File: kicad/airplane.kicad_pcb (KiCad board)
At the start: 2 copper layers, 23 parts, among them M1 Ailerons, M2 Elevator, M3 Rudder, M4 Wheel, U1 ESP32_DevKit, U10 L7805, U11 BMP280, U12 NEO-6M_GPS, U13 SD_Module, U2 nRF24L01+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

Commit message: airplane full pcb done
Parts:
- removed C5, C6: 10uF, Capacitor_THT:CP_Radial_D4.0mm_P1.50mm
- added G***: LOGO, airplane_foots:F18, F.Cu at (109.5, 84.2)
- added R1: 330, Resistor_THT:R_Axial_DIN0204_L3.6mm_D1.6mm_P5.08mm_Horizontal, F.Cu at (142.2, 116.5)
- added R2: 330, Resistor_THT:R_Axial_DIN0204_L3.6mm_D1.6mm_P5.08mm_Horizontal, F.Cu at (145.3, 116.5)
- added R3: 330, Resistor_THT:R_Axial_DIN0204_L3.6mm_D1.6mm_P5.08mm_Horizontal, F.Cu at (148.5, 116.5)
- added R4: 330, Resistor_THT:R_Axial_DIN0204_L3.6mm_D1.6mm_P5.08mm_Horizontal, F.Cu at (151.7, 116.5)
- U10: value L7805 -> AMS1117-3.3; footprint Package_TO_SOT_THT:TO-220-3_Vertical -> Connector_PinHeader_2.54mm:PinHeader_1x03_P2.54mm_Vertical
- moved U1 169.4 mm to (192.1, 111.8), turned to 90 degrees
- moved U3 158.2 mm to (200.7, 84.7)
- moved M1 155.1 mm to (178.7, 89.8), turned to 180 degrees
- moved U2 146.8 mm to (218.7, 87.8)
- moved M2 146.0 mm to (174.1, 89.8), turned to 180 degrees
- moved U4 142.6 mm to (189.7, 84.7)
- moved M3 136.9 mm to (169.5, 89.8), turned to 180 degrees
- moved M4 127.8 mm to (164.9, 89.8), turned to 180 degrees
- moved C1 106.6 mm to (154.0, 98.8)
- moved C2 101.2 mm to (154.2, 82.8)
- moved U8 99.0 mm to (126.7, 122.2)
- moved C3 94.2 mm to (144.7, 98.8)
- moved C4 90.5 mm to (144.7, 82.8)
- moved U13 70.6 mm to (113.2, 94.2), turned to 180 degrees
- moved U10 66.6 mm to (156.2, 108.8), turned to 180 degrees
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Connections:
- C1 pad 1: Net-(U10-IN) -> Net-(U10-VI)
- C3 pad 1: Net-(U10-IN) -> Net-(U10-VI)
- U10 pad 1: Net-(U10-IN) -> GND
- U10 pad 2: GND -> Net-(U10-VO)
- U10 pad 3: Net-(U10-OUT) -> Net-(U10-VI)
- U11 pad 1: Net-(U10-OUT) -> Net-(U10-VO)
- U11 pad 5: Net-(U10-OUT) -> Net-(U10-VO)
- U12 pad 1: Net-(U10-OUT) -> Net-(U10-VO)
- U13 pad 2: unconnected-(U13-3V3-Pad2) -> Net-(U10-VO)
- U13 pad 3: Net-(U10-OUT) -> unconnected-(U13-5V-Pad3)_1
- U5 pad 2: Net-(U10-IN) -> Net-(U10-VI)
- U6 pad 1: Net-(U10-IN) -> Net-(U10-VI)
- U6 pad 2: GND -> Net-(M1-+)
- U6 pad 3: Net-(M1-+) -> GND
- U7 pad 1: Net-(U10-IN) -> Net-(U10-VI)
- U7 pad 2: GND -> Net-(M3-+)
- U7 pad 3: Net-(M3-+) -> GND
- U8 pad 2: GND -> Net-(U8-GNDR)
- U8 pad 4: GND -> Net-(U8-GNDG)
- U8 pad 6: GND -> Net-(U8-GND1)
- U8 pad 8: GND -> Net-(U8-GND2)
- U9 pad 1: Net-(U10-OUT) -> Net-(U10-VO)
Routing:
- net Net-(U1-GPIO16): track 0.00 -> 137.5 mm
- net Net-(U1-GPIO17): track 0.00 -> 136.3 mm
- net Net-(U10-VO): track 0.00 -> 132.6 mm
- net Net-(U1-GPIO19): track 0.00 -> 103.2 mm, vias 0 -> 2
- net Net-(U1-GPIO18): track 0.00 -> 102.8 mm, vias 0 -> 1
- net Net-(U1-GPIO21): track 0.00 -> 95.5 mm
- net Net-(U1-GPIO22): track 0.00 -> 87.7 mm
- net Net-(U1-GPIO23): track 0.00 -> 83.7 mm, vias 0 -> 1
- net Net-(U1-GPIO5): track 0.00 -> 78.9 mm, vias 0 -> 1
- net Net-(U1-VIN): track 0.00 -> 73.4 mm
- net Net-(U10-VI): track 0.00 -> 73.2 mm
- net Net-(M1-PWM): track 0.00 -> 70.0 mm
- net Net-(U1-GPIO26): track 0.00 -> 70.0 mm, vias 0 -> 1
- net Net-(M2-PWM): track 0.00 -> 64.3 mm
- net Net-(M3-PWM): track 0.00 -> 63.7 mm
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- added copper zone on B.Cu, net GND
- added copper zone on F.Cu, net GND
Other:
- board outline added: 120 x 50 mm
- board text added: "Final Project - Airplane Breno Soares Alves"
- board text added: "M1: Ailerons - GPIO13 M2: Elevator - GPIO12 M3, M4: R&W - GPIO14 U4: PWM - GPIO15 U8: Nav - GPIO26 U8: Strobe - GPIO27 U13: CS - GPIO5 U2: CE - GPIO4 U2: CSN - GPIO15"

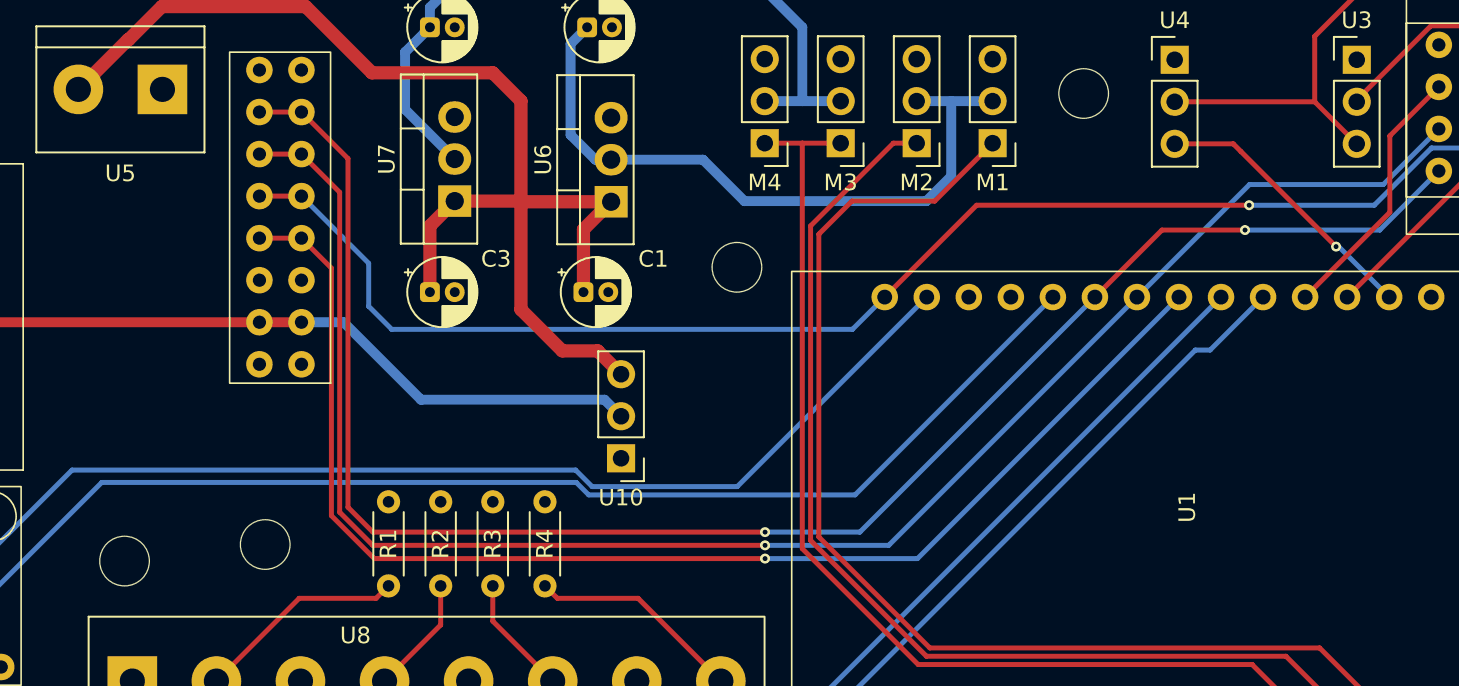
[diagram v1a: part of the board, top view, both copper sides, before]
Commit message: remote control schematic done, waiting revision
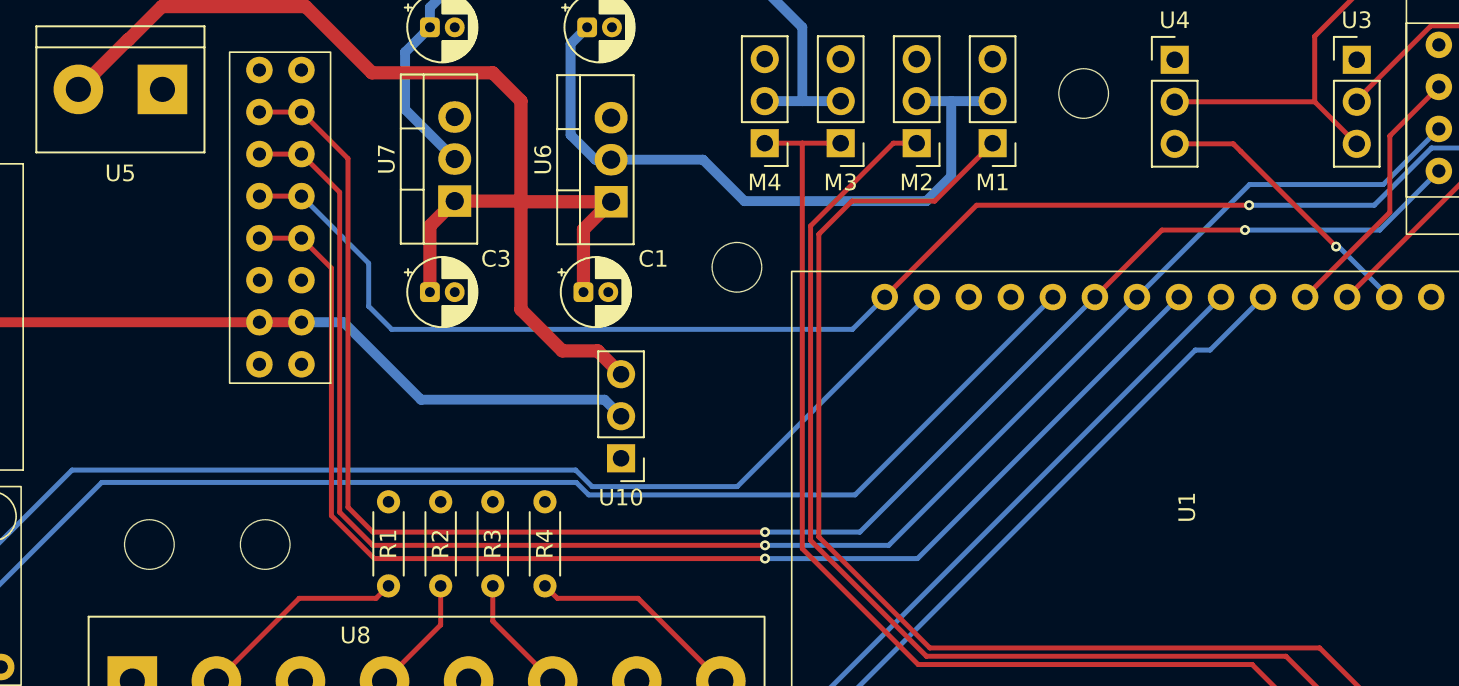
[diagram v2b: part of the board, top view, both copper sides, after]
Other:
- outline, holes or cut-outs redrawn
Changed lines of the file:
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@@
 		)
 		(embedded_fonts no)
+		(model "${KIPRJMOD}/3d/bmp280_module.stp"
+			(offset
+				(xyz 3.5 -4.75 27.5)
+			)
+			(scale
+				(xyz 1 1 1)
+			)
+			(rotate
+				(xyz -90 -0 90)
+			)
+		)
 	)
 	(footprint "Connector_PinHeader_2.54mm:PinHeader_1x03_P2.54mm_Vertical"
@@
 	)
 	(gr_circle
-		(center 126.25 115)
-		(end 127.75 115)
+		(center 127.75 114)
+		(end 129.25 114)
 		(stroke
 			(width 0.05)
@@
 	)
 	(segment
-		(start 198.16 87.25)
-		(end 189.7 87.25)
+		(start 210.2 121.99)
+		(end 210.2 82.25)
 		(width 0.3)
 		(layer "F.Cu")
@@
 	)
 	(segment
-		(start 210.2 121.99)
-		(end 210.2 82.25)
+		(start 189.7 87.25)
+		(end 198.16 87.25)
 		(width 0.3)
 		(layer "F.Cu")
@@
 	)
 	(segment
-		(start 200.7 89.79)
-		(end 198.16 87.25)
+		(start 207.74 124.45)
+		(end 210.2 121.99)
 		(width 0.3)
 		(layer "F.Cu")
@@
 	)
 	(segment
-		(start 207.74 124.45)
-		(end 210.2 121.99)
+		(start 198.16 87.25)
+		(end 200.7 89.79)
 		(width 0.3)
 		(layer "F.Cu")
@@
 	)
 	(segment
-		(start 207.049 82.659)
-		(end 208.2 83.81)
+		(start 200.7 87.25)
+		(end 200.7 87.14224)
 		(width 0.3)
 		(layer "F.Cu")
@@
 	)
 	(segment
-		(start 205.18324 82.659)
-		(end 207.049 82.659)
+		(start 200.7 87.14224)
+		(end 205.18324 82.659)
 		(width 0.3)
 		(layer "F.Cu")
@@
 	)
 	(segment
-		(start 200.7 87.14224)
-		(end 205.18324 82.659)
+		(start 207.049 82.659)
+		(end 208.2 83.81)
 		(width 0.3)
 		(layer "F.Cu")
@@
 	)
 	(segment
-		(start 200.7 87.25)
-		(end 200.7 87.14224)
+		(start 205.18324 82.659)
+		(end 207.049 82.659)
 		(width 0.3)
 		(layer "F.Cu")
@@
 	)
 	(segment
+		(start 134.4 100.57)
+		(end 112.52 100.57)
+		(width 0.6)
+		(layer "F.Cu")
+		(net 42)
+	)
+	(segment
 		(start 98 125.99)
 		(end 94.2 122.19)
@@
 	)
 	(segment
-		(start 94.2 122.19)
-		(end 94.2 90.13)
-		(width 0.6)
-		(layer "F.Cu")
-		(net 42)
-	)
-	(segment
 		(start 112.52 100.57)
 		(end 99.08 87.13)
@@
 	)
 	(segment
-		(start 106.1 125.15)
-		(end 106.1 121.4)
+		(start 94.2 122.19)
+		(end 94.2 90.13)
 		(width 0.6)
 		(layer "F.Cu")
@@
 	)
 	(segment
-		(start 99.08 87.13)
-		(end 97.2 87.13)
+		(start 106.1 125.15)
+		(end 106.1 121.4)
 		(width 0.6)
 		(layer "F.Cu")
@@
 	)
 	(segment
-		(start 134.4 100.57)
-		(end 112.52 100.57)
+		(start 99.08 87.13)
+		(end 97.2 87.13)
 		(width 0.6)
 		(layer "F.Cu")

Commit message: fabrication files created, waiting revision yet
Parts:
- added R5: 1k, Resistor_THT:R_Axial_DIN0204_L3.6mm_D1.6mm_P5.08mm_Horizontal, F.Cu at (122.7, 107.6)
- added R6: 620, Resistor_THT:R_Axial_DIN0204_L3.6mm_D1.6mm_P5.08mm_Horizontal, F.Cu at (125.8, 107.6)
- added R7: 2k2, Resistor_THT:R_Axial_DIN0204_L3.6mm_D1.6mm_P5.08mm_Horizontal, F.Cu at (129.0, 102.5)
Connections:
- U1 pad 8: unconnected-(U1-GPIO25-Pad8) -> Net-(U1-GPIO25)
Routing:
- net Net-(U1-GPIO25): track 0.00 -> 92.3 mm, vias 0 -> 1
- net Net-(U10-VI): track 73.2 -> 91.5 mm
- net Net-(R6-Pad1): track 0.00 -> 3.15 mm
